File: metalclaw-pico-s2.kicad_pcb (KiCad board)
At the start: 2 copper layers, 49 parts, among them J1 USB_C_Receptacle_USB2.0_14P, J2 Conn_01x05, J3 Conn_02x05_Odd_Even, U1 ESP32-S2, U2 MX25L3236FM2I-08G-TR, U3 APS6404L-3SQRx-SN, U5 XC6220B331MR, Y1 XRCGB40M000F1S2FR0

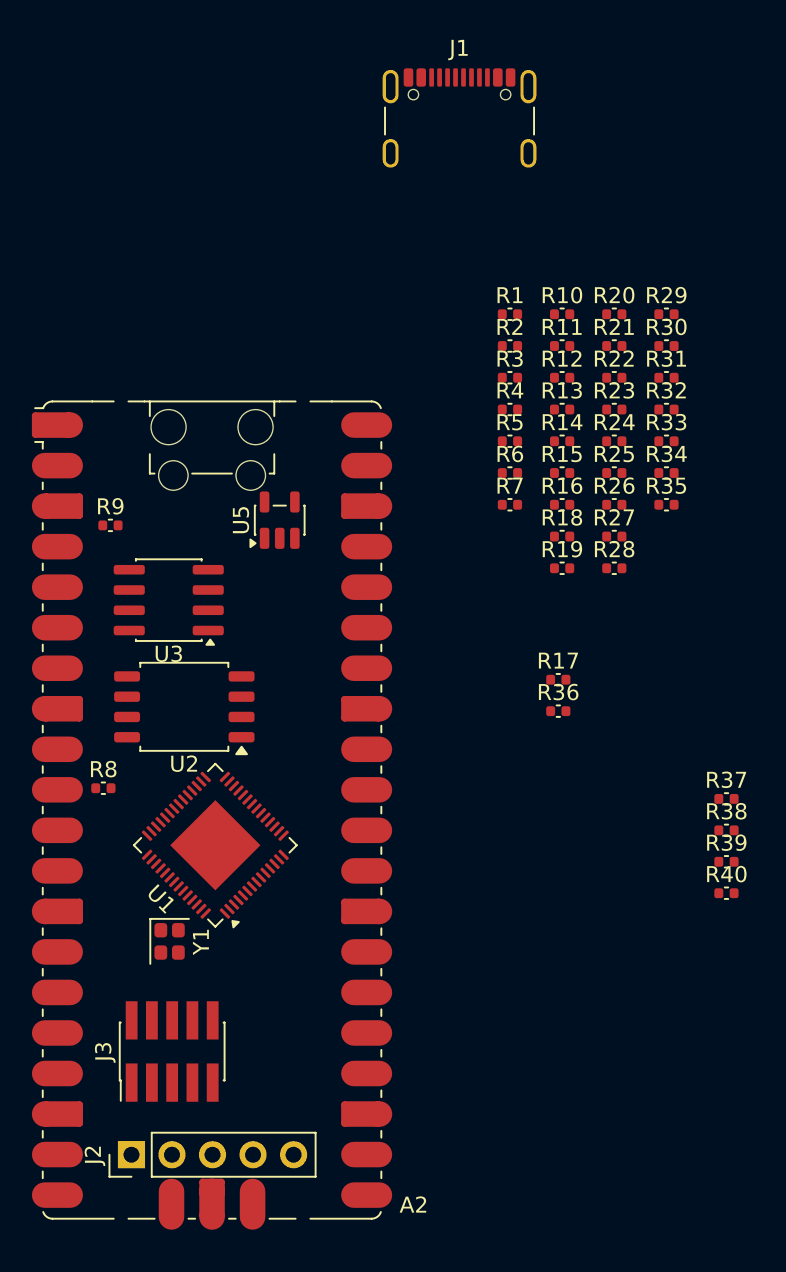
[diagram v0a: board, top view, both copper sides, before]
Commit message: Add footprint and parts for caps
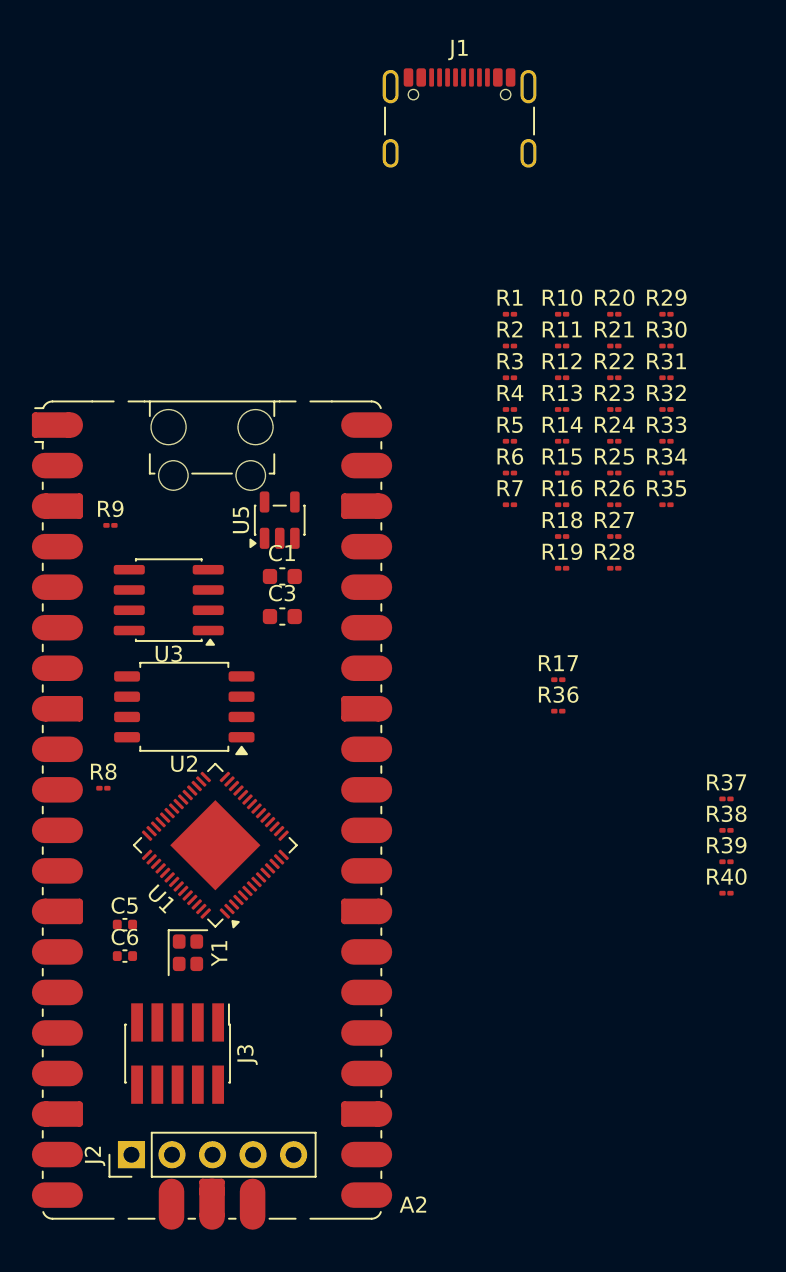
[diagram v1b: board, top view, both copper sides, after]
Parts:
- added C1: 10u, Capacitor_SMD:C_0603_1608Metric, F.Cu at (168.2, 84.2)
- added C3: 10u, Capacitor_SMD:C_0603_1608Metric, F.Cu at (168.2, 86.7)
- added C5: 6p, Capacitor_SMD:C_0402_1005Metric, F.Cu at (158.3, 106.0)
- added C6: 6p, Capacitor_SMD:C_0402_1005Metric, F.Cu at (158.3, 108.0)
- R1, R10, R11, R12, R13, R14, R15, R16, R17, R18, R19, R2, R20, R21, R22, R23, R24, R25, R26, R27, R28, R29, R3, R30, R31, R32, R33, R34, R35, R36, R37, R38, R39, R4, R40, R5, R6, R7, R8, R9: footprint Capacitor_SMD:C_0402_1005Metric -> Resistor_SMD:R_01005_0402Metric
- moved Y1 1.35 mm to (162.3, 107.8)
- moved J3 0.36 mm to (161.7, 114.1), turned to -90 degrees

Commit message: Place resistors in rough areas
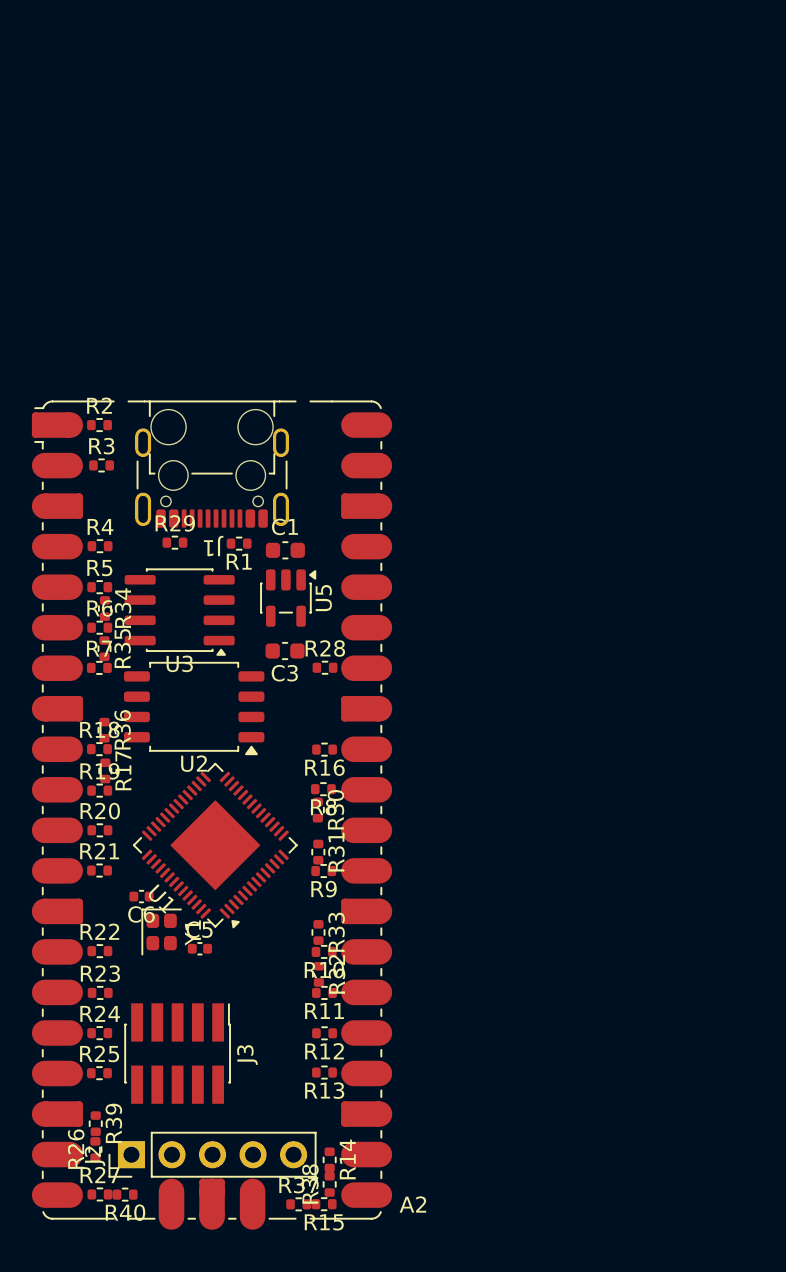
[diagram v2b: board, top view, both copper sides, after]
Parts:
- R1, R10, R11, R12, R13, R14, R15, R16, R17, R18, R19, R2, R20, R21, R22, R23, R24, R25, R26, R27, R28, R29, R3, R30, R31, R32, R33, R34, R35, R36, R37, R38, R39, R4, R40, R5, R6, R7, R8, R9: footprint Resistor_SMD:R_01005_0402Metric -> Resistor_SMD:R_0402_1005Metric
- moved R27 52.3 mm to (156.8, 123.0)
- moved R26 51.9 mm to (156.5, 120.1), turned to 90 degrees
- moved R25 49.6 mm to (156.8, 115.4)
- moved R24 49.2 mm to (156.8, 112.8)
- moved R23 48.7 mm to (156.8, 110.3)
- moved R22 48.3 mm to (156.8, 107.7)
- moved R15 48.2 mm to (170.8, 123.6), turned to 180 degrees
- moved R14 47.3 mm to (171.2, 120.8), turned to -90 degrees
- moved R21 46.1 mm to (156.8, 102.7)
- moved R20 45.7 mm to (156.8, 100.1)
- moved R13 44.1 mm to (170.9, 115.3), turned to 180 degrees
- moved R12 43.7 mm to (170.9, 112.9), turned to 180 degrees
- moved R11 43.2 mm to (170.9, 110.3), turned to 180 degrees
- moved R39 42.8 mm to (156.5, 118.5), turned to -90 degrees
- moved R10 42.7 mm to (170.8, 107.8), turned to 180 degrees
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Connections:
- J1 pad B6: /GP28 -> Net-(U1-GPIO20/USB_D+)
- Y1 pad 1: Net-(U1-XTAL_P) -> Net-(U1-XTAL_N)
- Y1 pad 3: Net-(U1-XTAL_N) -> Net-(U1-XTAL_P)

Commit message: Rearrange pins to fit Pi Pico layout
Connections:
- R31 pad 2: /GP22 -> /GP15
- U1 pad 10: /GP4 -> /GP20
- U1 pad 11: /GP5 -> /GP21
- U1 pad 12: /GP6 -> /GP22
- U1 pad 13: /GP7 -> /GP0
- U1 pad 14: /GP8 -> /GP1
- U1 pad 15: /GP9 -> /GP2
- U1 pad 16: /GP10 -> /GP3
- U1 pad 17: /GP11 -> /GP4
- U1 pad 18: /GP12 -> /GP5
- U1 pad 19: /GP13 -> /GP6
- U1 pad 21: /GP14 -> /GP7
- U1 pad 22: /GP15 -> /GP8
- U1 pad 37: /GP16 -> /GP9
- U1 pad 38: /GP17 -> /GP10
- U1 pad 39: /GP18 -> /GP11
- U1 pad 40: /GP19 -> /GP12
- U1 pad 41: /GP21 -> /GP14
- U1 pad 42: /GP20 -> /GP13
- U1 pad 55: /GP22 -> /GP15
- U1 pad 6: /GP0 -> /GP16
- U1 pad 7: /GP1 -> /GP17
- U1 pad 8: /GP2 -> /GP18
- U1 pad 9: /GP3 -> /GP19
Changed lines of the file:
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@@
 			(layers "F.Cu" "F.Mask" "F.Paste")
 			(roundrect_rratio 0.25)
-			(net 48 "/GP22")
+			(net 47 "/GP15")
 			(pintype "passive")
 		)
@@
 			(layers "F.Cu" "F.Mask" "F.Paste")
 			(roundrect_rratio 0.25)
-			(net 76 "/GP0")
+			(net 71 "/GP16")
 			(pinfunction "GPIO1")
 			(pintype "bidirectional")
@@
 			(layers "F.Cu" "F.Mask" "F.Paste")
 			(roundrect_rratio 0.25)
-			(net 68 "/GP1")
+			(net 44 "/GP17")
 			(pinfunction "GPIO2")
 			(pintype "bidirectional")
@@
 			(layers "F.Cu" "F.Mask" "F.Paste")
 			(roundrect_rratio 0.25)
-			(net 69 "/GP2")
+			(net 51 "/GP18")
 			(pinfunction "GPIO3")
 			(pintype "bidirectional")
@@
 			(layers "F.Cu" "F.Mask" "F.Paste")
 			(roundrect_rratio 0.25)
-			(net 70 "/GP3")
+			(net 63 "/GP19")
 			(pinfunction "GPIO4")
 			(pintype "bidirectional")
@@
 			(layers "F.Cu" "F.Mask" "F.Paste")
 			(roundrect_rratio 0.25)
-			(net 66 "/GP4")
+			(net 45 "/GP20")
 			(pinfunction "GPIO5")
 			(pintype "bidirectional")
@@
 			(layers "F.Cu" "F.Mask" "F.Paste")
 			(roundrect_rratio 0.25)
-			(net 58 "/GP5")
+			(net 60 "/GP21")
 			(pinfunction "GPIO6")
 			(pintype "bidirectional")
@@
 			(layers "F.Cu" "F.Mask" "F.Paste")
 			(roundrect_rratio 0.25)
-			(net 50 "/GP6")
+			(net 48 "/GP22")
 			(pinfunction "GPIO7")
 			(pintype "bidirectional")
@@
 			(layers "F.Cu" "F.Mask" "F.Paste")
 			(roundrect_rratio 0.25)
-			(net 59 "/GP7")
+			(net 76 "/GP0")
 			(pinfunction "GPIO8")
 			(pintype "bidirectional")
@@
 			(layers "F.Cu" "F.Mask" "F.Paste")
 			(roundrect_rratio 0.25)
-			(net 74 "/GP8")
+			(net 68 "/GP1")
 			(pinfunction "GPIO9")
 			(pintype "bidirectional")
@@
 			(layers "F.Cu" "F.Mask" "F.Paste")
 			(roundrect_rratio 0.25)
-			(net 55 "/GP9")
+			(net 69 "/GP2")
 			(pinfunction "GPIO10")
 			(pintype "bidirectional")
@@
 			(layers "F.Cu" "F.Mask" "F.Paste")
 			(roundrect_rratio 0.25)
-			(net 62 "/GP10")
+			(net 70 "/GP3")
 			(pinfunction "GPIO11")
 			(pintype "bidirectional")
@@
 			(layers "F.Cu" "F.Mask" "F.Paste")
 			(roundrect_rratio 0.25)
-			(net 46 "/GP11")
+			(net 66 "/GP4")
 			(pinfunction "GPIO12")
 			(pintype "bidirectional")
@@
 			(layers "F.Cu" "F.Mask" "F.Paste")
 			(roundrect_rratio 0.25)
-			(net 64 "/GP12")
+			(net 58 "/GP5")
 			(pinfunction "GPIO13")
 			(pintype "bidirectional")
@@
 			(layers "F.Cu" "F.Mask" "F.Paste")
 			(roundrect_rratio 0.25)
-			(net 52 "/GP13")
+			(net 50 "/GP6")
 			(pinfunction "GPIO14")
 			(pintype "bidirectional")
@@
 			(layers "F.Cu" "F.Mask" "F.Paste")
 			(roundrect_rratio 0.25)
-			(net 77 "/GP14")
+			(net 59 "/GP7")
 			(pinfunction "XTAL_32K_P")
 			(pintype "passive")
@@
 			(layers "F.Cu" "F.Mask" "F.Paste")
 			(roundrect_rratio 0.25)
-			(net 47 "/GP15")
+			(net 74 "/GP8")
 			(pinfunction "XTAL_32K_N")
 			(pintype "passive")
@@
 			(layers "F.Cu" "F.Mask" "F.Paste")
 			(roundrect_rratio 0.25)
-			(net 71 "/GP16")
+			(net 55 "/GP9")
 			(pinfunction "GPIO33")
 			(pintype "bidirectional")
@@
 			(layers "F.Cu" "F.Mask" "F.Paste")
 			(roundrect_rratio 0.25)
-			(net 44 "/GP17")
+			(net 62 "/GP10")
 			(pinfunction "GPIO34")
 			(pintype "bidirectional")
@@
 			(layers "F.Cu" "F.Mask" "F.Paste")
 			(roundrect_rratio 0.25)
-			(net 51 "/GP18")
+			(net 46 "/GP11")
 			(pinfunction "GPIO35")
 			(pintype "bidirectional")
@@
 			(layers "F.Cu" "F.Mask" "F.Paste")
 			(roundrect_rratio 0.25)
-			(net 63 "/GP19")
+			(net 64 "/GP12")
 			(pinfunction "GPIO36")
 			(pintype "bidirectional")
@@
 			(layers "F.Cu" "F.Mask" "F.Paste")
 			(roundrect_rratio 0.25)
-			(net 60 "/GP21")
+			(net 77 "/GP14")
 			(pinfunction "GPIO37")
 			(pintype "bidirectional")
@@
 			(layers "F.Cu" "F.Mask" "F.Paste")
 			(roundrect_rratio 0.25)
-			(net 45 "/GP20")
+			(net 52 "/GP13")
 			(pinfunction "GPIO38")
 			(pintype "bidirectional")
@@
 			(layers "F.Cu" "F.Mask" "F.Paste")
 			(roundrect_rratio 0.25)
-			(net 48 "/GP22")
+			(net 47 "/GP15")
 			(pinfunction "GPIO46")
 			(pintype "input")
@@
 			(net 2 "unconnected-(U1-CHIP_PU-Pad56)")
 			(pinfunction "CHIP_PU")
-			(pintype "input")
+			(pintype "input+no_connect")
 		)
 		(pad "57" smd rect

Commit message: Add initial Pi Pico footprint
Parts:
- A2: footprint Module:RaspberryPi_Pico_SMD_HandSolder -> MetalClaw:RaspberryPi_Pico_SMD

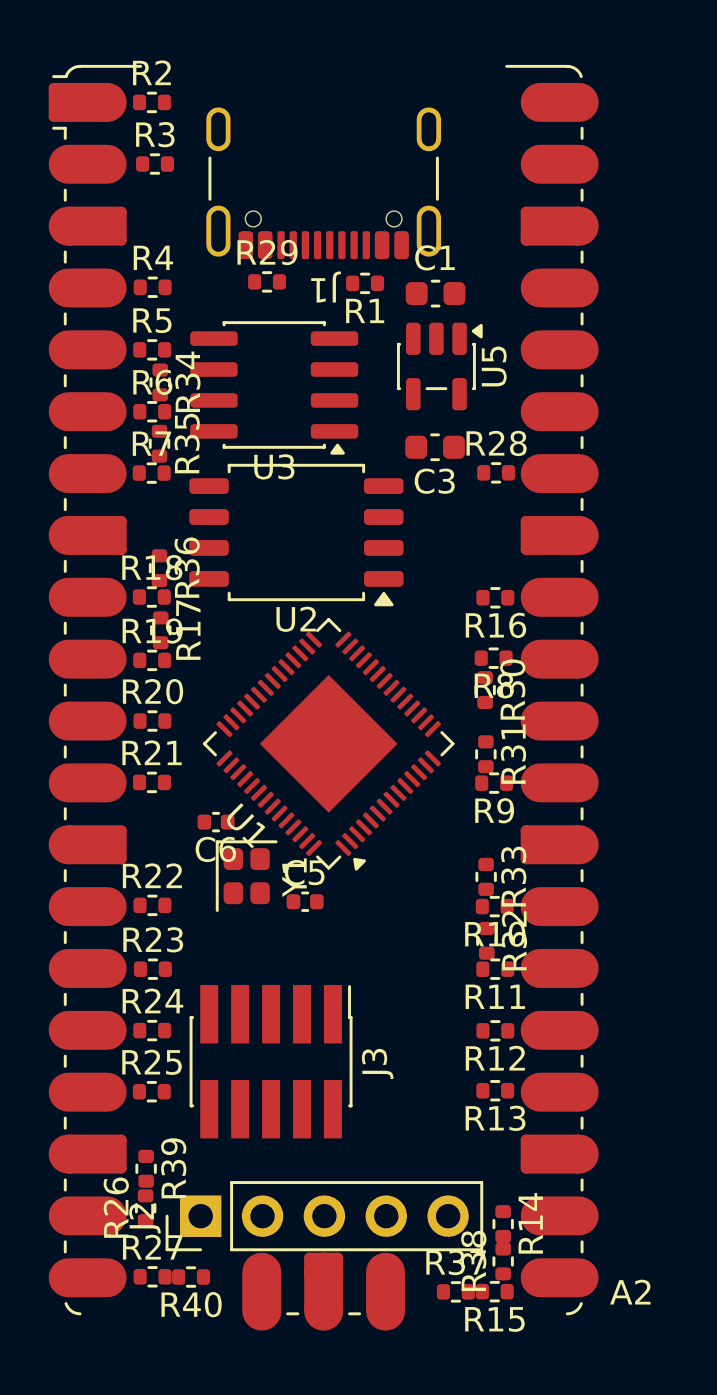
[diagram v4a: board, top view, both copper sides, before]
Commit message: Further refine Pi Pico footprint
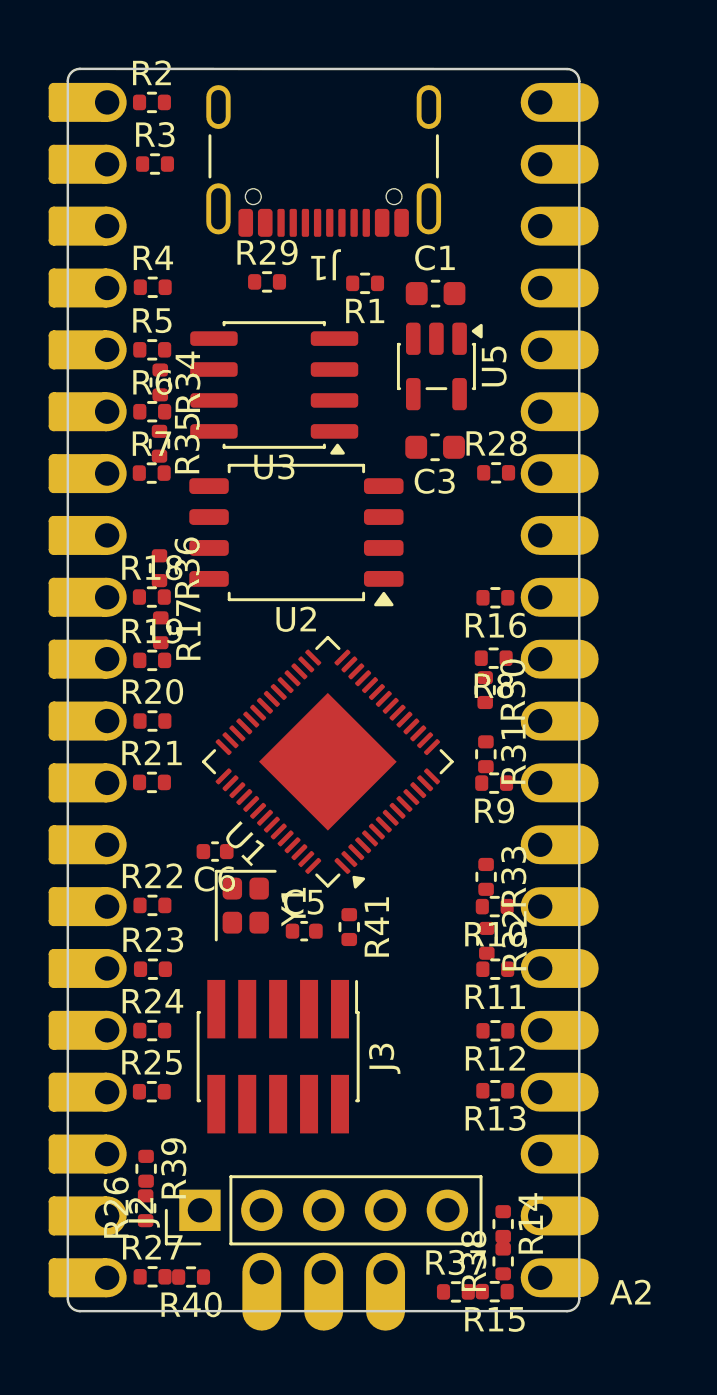
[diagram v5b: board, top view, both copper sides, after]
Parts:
- added R41: 5.1k, Resistor_SMD:R_0402_1005Metric, F.Cu at (164.9, 108.6)
- moved C5 1.21 mm to (163.0, 108.8)
- moved C6 1.21 mm to (159.3, 105.5)
- moved Y1 1.21 mm to (160.6, 107.7)
- moved J1 0.92 mm to (163.8, 76.0)
- moved U1 0.74 mm to (164.0, 101.8)
- moved J3 0.36 mm to (161.9, 113.9)
- moved J2 0.24 mm to (158.7, 120.2)
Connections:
- J2 pad 5: GND -> Net-(J2-Pin_5)
- U1 pad 56: unconnected-(U1-CHIP_PU-Pad56) -> Net-(J2-Pin_5)
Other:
- board outline added: 21 x 51 mm
